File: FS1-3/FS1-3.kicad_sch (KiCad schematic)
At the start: 42 parts

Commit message: cleaning up references
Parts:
- renumbered 1A_FS1_ to 1A_FS1, 1A_FS2_ to 1A_FS2, 1B_FS1_ to 1B_FS1, 1B_FS2_ to 1B_FS2, 1C_FS1_ to 1C_FS1, 1C_FS2_ to 1C_FS2, 1D_FS1_ to 1D_FS1, 1D_FS2_ to 1D_FS2, 1E_FS1_ to 1E_FS1, 1E_FS2_ to 1E_FS2, 1F_FS1_ to 1F_FS1, 1F_FS2_ to 1F_FS2, 2C_FS1_ to 2C_FS1, 2C_FS2_ to 2C_FS2, 3A_FS1_ to 3A_FS1, 3A_FS2_ to 3A_FS2, 3B_FS1_ to 3B_FS1, 3B_FS2_ to 3B_FS2, 3C_FS1_ to 3C_FS1, 3C_FS2_ to 3C_FS2, 3D_FS1_ to 3D_FS1, 3D_FS2_ to 3D_FS2, 3E_FS1_ to 3E_FS1, 3E_FS2_ to 3E_FS2, 3F_FS1_ to 3F_FS1, 3F_FS2_ to 3F_FS2, 4C_FS1_ to 4C_FS1, 4C_FS2_ to 4C_FS2, 5A_FS1_ to 5A_FS1, 5A_FS2_ to 5A_FS2, 5B_FS1_ to 5B_FS1, 5B_FS2_ to 5B_FS2, 5C_FS1_ to 5C_FS1, 5C_FS2_ to 5C_FS2, 5D_FS1_ to 5D_FS1, 5D_FS2_ to 5D_FS2, 5E_FS1_ to 5E_FS1, 5E_FS2_ to 5E_FS2, 5F_FS1_ to 5F_FS1, 5F_FS2_ to 5F_FS2

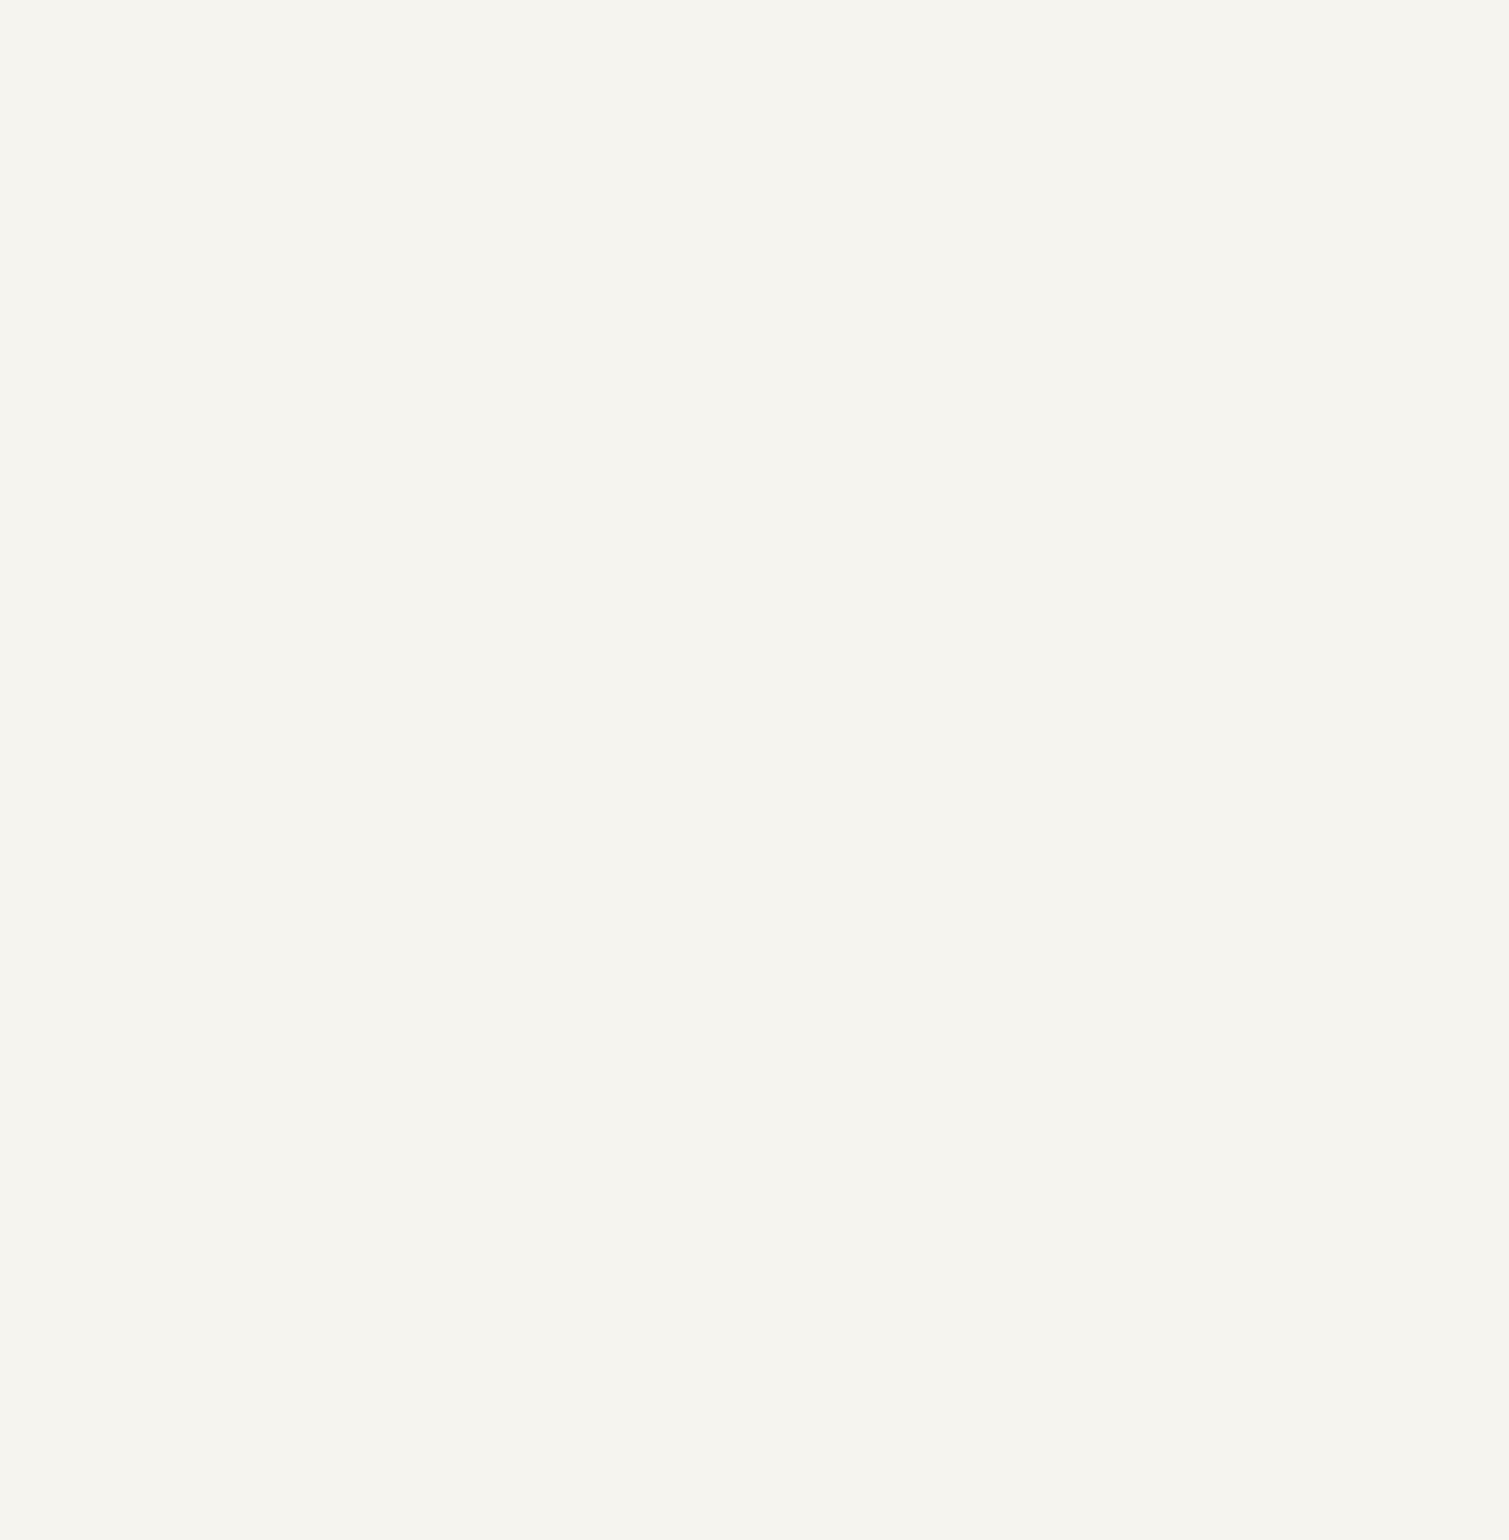
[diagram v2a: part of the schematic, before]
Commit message: addressing a few more ERC errors
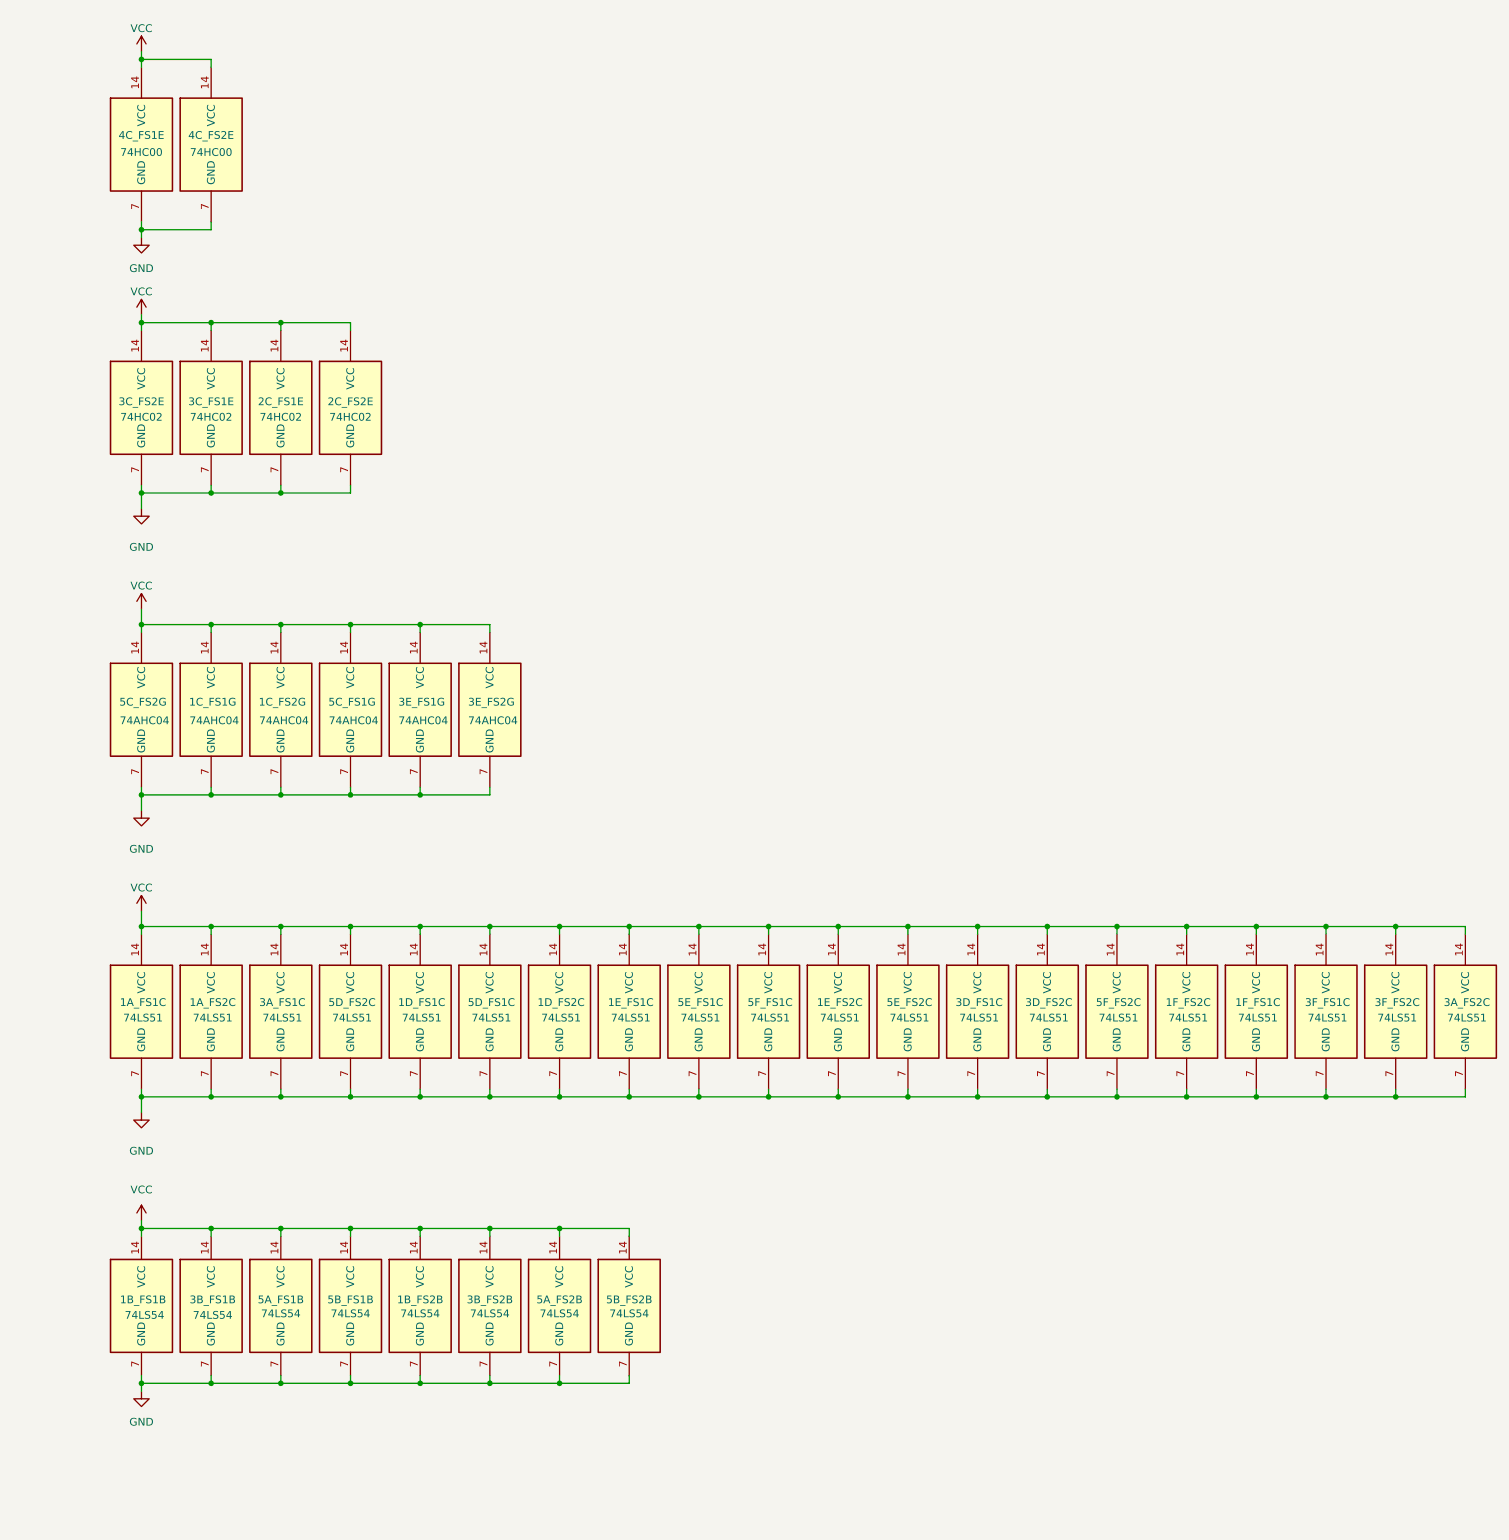
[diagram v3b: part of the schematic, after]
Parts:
- added unit 3 of 1A_FS1
- added unit 3 of 1A_FS2
- added unit 2 of 1B_FS1
- added unit 2 of 1B_FS2
- added unit 7 of 1C_FS1
- added unit 7 of 1C_FS2
- added unit 3 of 1D_FS1
- added unit 3 of 1D_FS2
- added unit 3 of 1E_FS1
- added unit 3 of 1E_FS2
- added unit 3 of 1F_FS1
- added unit 3 of 1F_FS2
- added unit 5 of 2C_FS1
- added unit 5 of 2C_FS2
- added unit 3 of 3A_FS1
- added unit 3 of 3A_FS2
- added unit 2 of 3B_FS1
- added unit 2 of 3B_FS2
- added unit 5 of 3C_FS1
- added unit 5 of 3C_FS2
- added unit 3 of 3D_FS1
- added unit 3 of 3D_FS2
- added unit 7 of 3E_FS1
- added unit 7 of 3E_FS2
- added unit 3 of 3F_FS1
- added unit 3 of 3F_FS2
- added unit 5 of 4C_FS1
- added unit 5 of 4C_FS2
- added unit 2 of 5A_FS1
- added unit 2 of 5A_FS2
- added unit 2 of 5B_FS1
- added unit 2 of 5B_FS2
- added unit 7 of 5C_FS1
- added unit 7 of 5C_FS2
- added unit 3 of 5D_FS1
- added unit 3 of 5D_FS2
- added unit 3 of 5E_FS1
- added unit 3 of 5E_FS2
- added unit 3 of 5F_FS1
- added unit 3 of 5F_FS2
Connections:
- net GND: now also 1A_FS1.7 (GND), 1A_FS2.7 (GND), 1B_FS1.7 (GND), 1B_FS2.7 (GND), 1C_FS1.7 (GND), 1C_FS2.7 (GND), 1D_FS1.7 (GND), 1D_FS2.7 (GND), 1E_FS1.7 (GND), 1E_FS2.7 (GND), 1F_FS1.7 (GND), 1F_FS2.7 (GND), 2C_FS1.7 (GND), 2C_FS2.7 (GND), 3A_FS1.7 (GND), 3A_FS2.7 (GND), 3B_FS1.7 (GND), 3B_FS2.7 (GND), 3C_FS1.7 (GND), 3C_FS2.7 (GND), 3D_FS1.7 (GND), 3D_FS2.7 (GND), 3E_FS1.7 (GND), 3E_FS2.7 (GND), 3F_FS1.7 (GND), 3F_FS2.7 (GND), 4C_FS1.7 (GND), 4C_FS2.7 (GND), 5A_FS1.7 (GND), 5A_FS2.7 (GND), 5B_FS1.7 (GND), 5B_FS2.7 (GND), 5C_FS1.7 (GND), 5C_FS2.7 (GND), 5D_FS1.7 (GND), 5D_FS2.7 (GND), 5E_FS1.7 (GND), 5E_FS2.7 (GND), 5F_FS1.7 (GND), 5F_FS2.7 (GND)
- net VCC: now also 1A_FS1.14 (VCC), 1A_FS2.14 (VCC), 1B_FS1.14 (VCC), 1B_FS2.14 (VCC), 1C_FS1.14 (VCC), 1C_FS2.14 (VCC), 1D_FS1.14 (VCC), 1D_FS2.14 (VCC), 1E_FS1.14 (VCC), 1E_FS2.14 (VCC), 1F_FS1.14 (VCC), 1F_FS2.14 (VCC), 2C_FS1.14 (VCC), 2C_FS2.14 (VCC), 3A_FS1.14 (VCC), 3A_FS2.14 (VCC), 3B_FS1.14 (VCC), 3B_FS2.14 (VCC), 3C_FS1.14 (VCC), 3C_FS2.14 (VCC), 3D_FS1.14 (VCC), 3D_FS2.14 (VCC), 3E_FS1.14 (VCC), 3E_FS2.14 (VCC), 3F_FS1.14 (VCC), 3F_FS2.14 (VCC), 4C_FS1.14 (VCC), 4C_FS2.14 (VCC), 5A_FS1.14 (VCC), 5A_FS2.14 (VCC), 5B_FS1.14 (VCC), 5B_FS2.14 (VCC), 5C_FS1.14 (VCC), 5C_FS2.14 (VCC), 5D_FS1.14 (VCC), 5D_FS2.14 (VCC), 5E_FS1.14 (VCC), 5E_FS2.14 (VCC), 5F_FS1.14 (VCC), 5F_FS2.14 (VCC)
